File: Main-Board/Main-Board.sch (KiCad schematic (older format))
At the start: 1 part

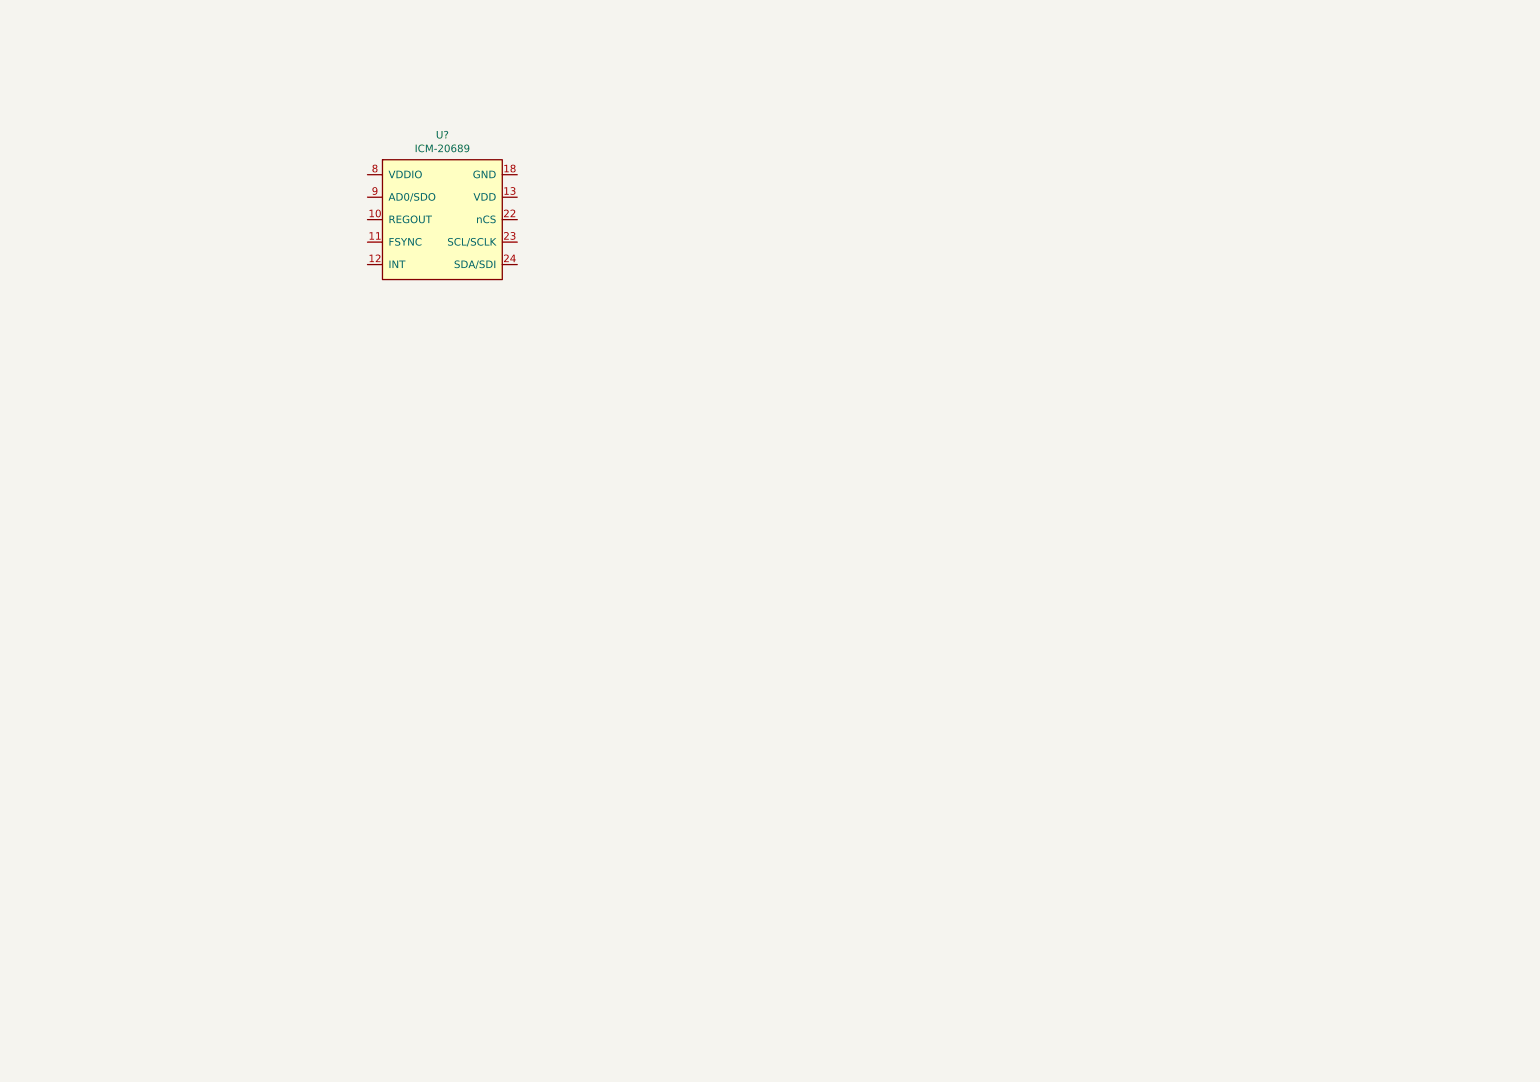
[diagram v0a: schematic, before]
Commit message: roughed out the imu schematic
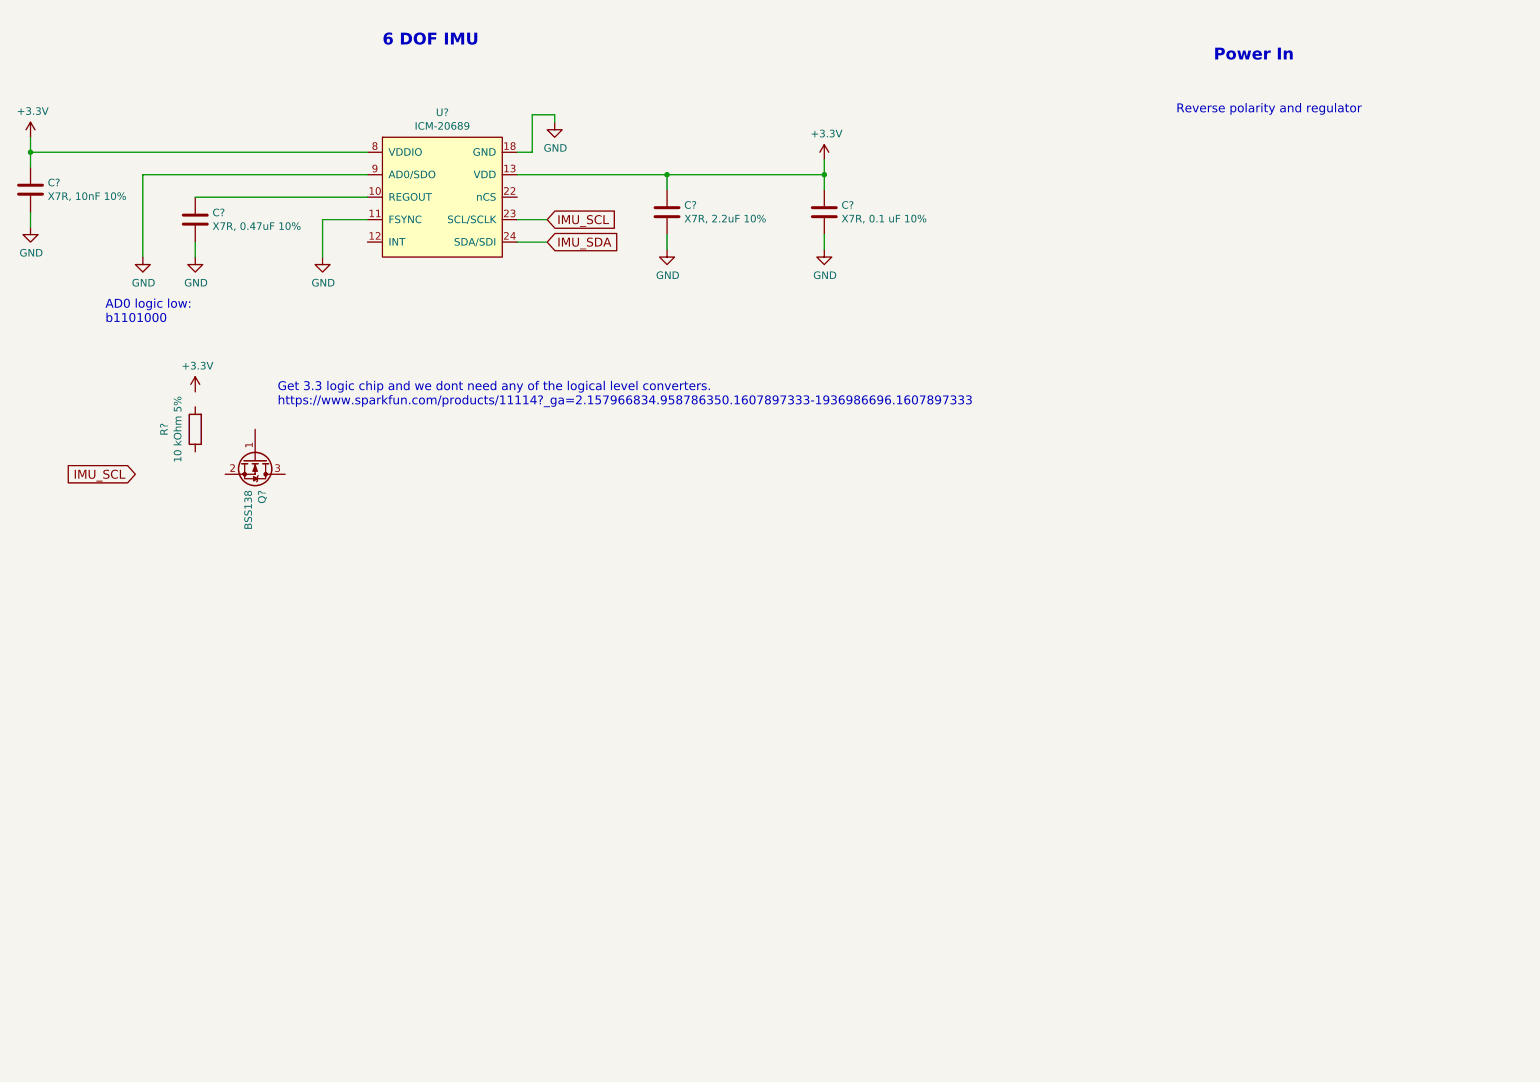
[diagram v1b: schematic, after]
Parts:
- added C?: X7R, 0.47uF 10%, Capacitor_SMD:C_0603_1608Metric_Pad1.05x0.95mm_HandSolder, symbol Device:C
- added C?: X7R, 0.1 uF 10%, Capacitor_SMD:C_0603_1608Metric_Pad1.05x0.95mm_HandSolder, symbol Device:C
- added C?: X7R, 2.2uF 10%, Capacitor_SMD:C_0603_1608Metric_Pad1.05x0.95mm_HandSolder, symbol Device:C
- added C?: X7R, 10nF 10%, Capacitor_SMD:C_0603_1608Metric_Pad1.05x0.95mm_HandSolder, symbol Device:C
- added Q?: BSS138, Package_TO_SOT_SMD:SOT-23, symbol Transistor_FET:BSS138
- added R?: 10 kOhm 5%, symbol Device:R
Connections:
- net at U?.10 (REGOUT): now also C?.1
- net GND: now reaches U?.11 (FSYNC)
- net GND: now also U?.18 (GND), U?.9 (AD0/SDO), C?.2, C?.2, C?.2, C?.2
- net +3V3: now reaches U?.13 (VDD)
- net +3V3: now also U?.8 (VDDIO), C?.1, C?.1, C?.1
- net IMU_SCL: now reaches U?.23 (SCL/SCLK)
- net IMU_SDA: now reaches U?.24 (SDA/SDI)
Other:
- note added: "6 DOF IMU"
- note added: "AD0 logic low: \nb1101000"
- note added: "Get 3.3 logic chip and we dont need any of the logical level converters. \nhttps://www.sparkfun.com/products/11114?_ga=2.157966834.958786350.1607897333-1936986696.1607897333"
- note added: "Power In"
- note added: "Reverse polarity and regulator"
- moved on the sheet: U?

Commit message: Select ATMEGA328P as main processor, started to route.
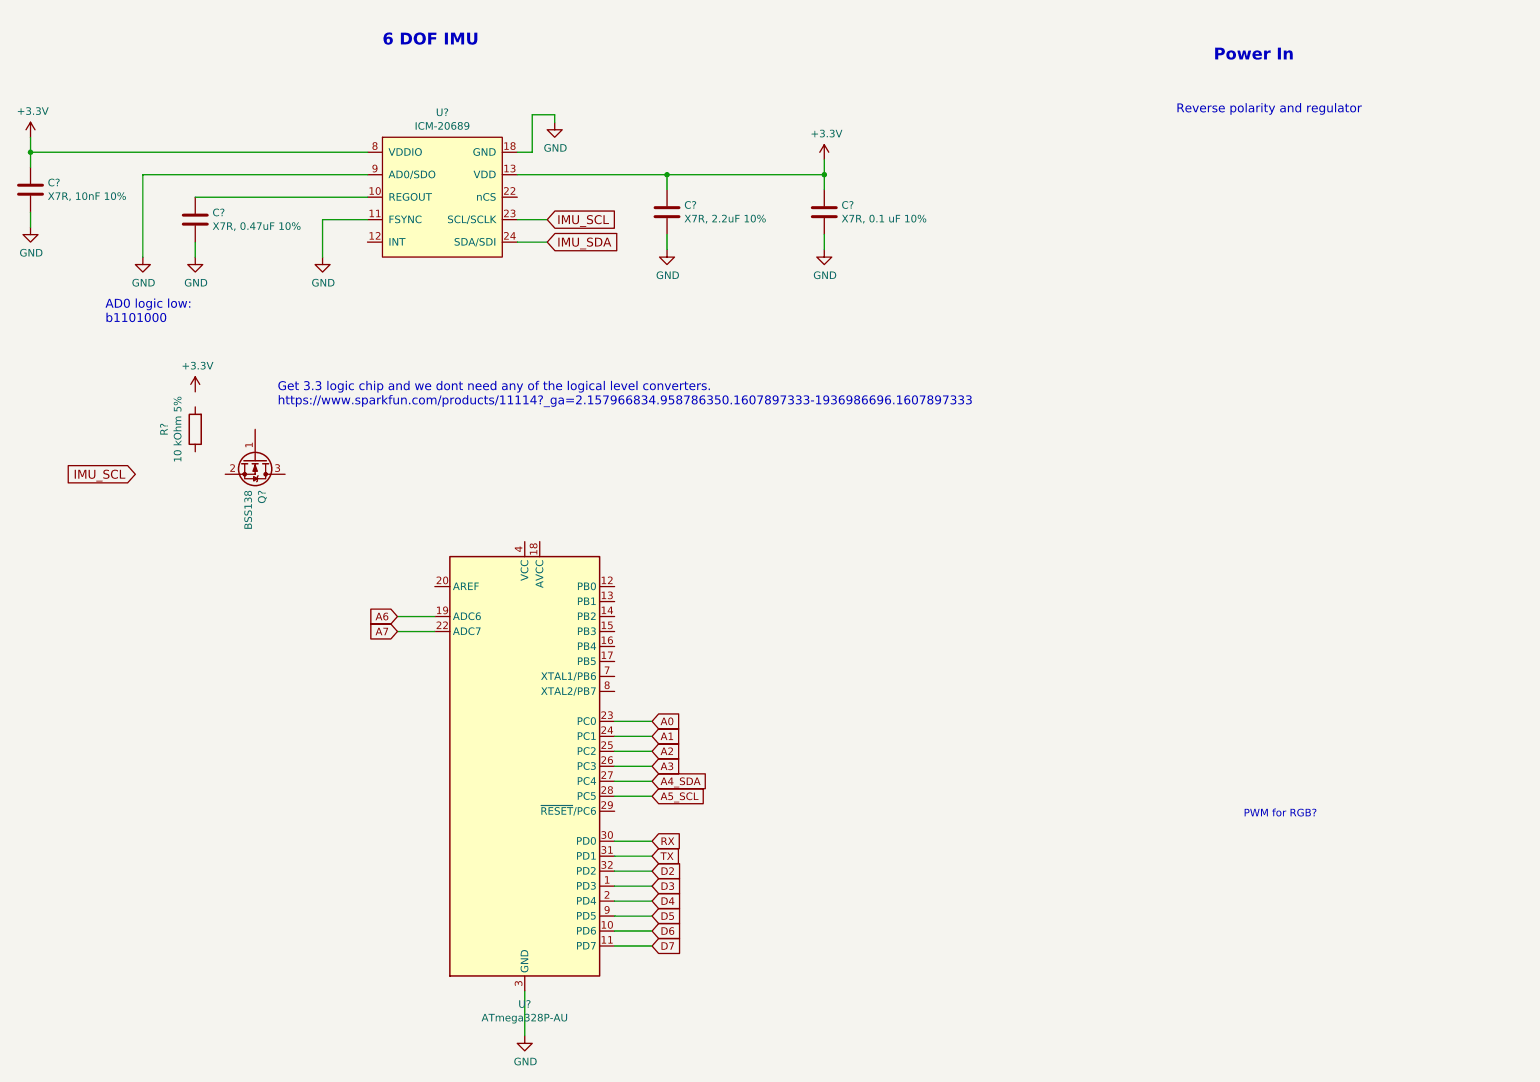
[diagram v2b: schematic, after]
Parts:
- added U?: ATmega328P-AU, Package_QFP:TQFP-32_7x7mm_P0.8mm, symbol MCU_Microchip_ATmega:ATmega328P-AU
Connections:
- net GND: now also U?.21 (GND), U?.3 (GND), U?.5 (GND)
- new net: U?.4 (VCC), U?.6 (VCC)
- new net A0: U?.23 (PC0)
- new net A1: U?.24 (PC1)
- new net A2: U?.25 (PC2)
- new net A3: U?.26 (PC3)
- new net A4_SDA: U?.27 (PC4)
- new net A5_SCL: U?.28 (PC5)
- new net A6: U?.19 (ADC6)
- new net A7: U?.22 (ADC7)
- new net D2: U?.32 (PD2)
- new net D3: U?.1 (PD3)
- new net D4: U?.2 (PD4)
- new net D5: U?.9 (PD5)
- new net D6: U?.10 (PD6)
- new net D7: U?.11 (PD7)
- new net RX: U?.30 (PD0)
- new net TX: U?.31 (PD1)
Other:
- note added: "PWM for RGB?"
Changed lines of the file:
@@
 EESchema Schematic File Version 4
+LIBS:Main-Board-cache
 EELAYER 30 0
 EELAYER END
@@
 Text Notes 2300 3250 0    59   ~ 0
 Get 3.3 logic chip and we dont need any of the logical level converters. \nhttps://www.sparkfun.com/products/11114?_ga=2.157966834.958786350.1607897333-1936986696.1607897333
+$Comp
+L MCU_Microchip_ATmega:ATmega328P-AU U?
+U 1 1 5FD850AB
+P 3950 5650
+F 0 "U?" H 3950 4061 50  0000 C CNN
+F 1 "ATmega328P-AU" H 3950 3970 50  0000 C CNN
+F 2 "Package_QFP:TQFP-32_7x7mm_P0.8mm" H 3950 5650 50  0001 C CIN
+F 3 "http://ww1.microchip.com/downloads/en/DeviceDoc/ATmega328_P%20AVR%20MCU%20with%20picoPower%20Technology%20Data%20Sheet%2040001984A.pdf" H 3950 5650 50  0001 C CNN
+	1    3950 5650
+	1    0    0    -1
+$EndComp
+Text GLabel 4800 5350 2    50   Input ~ 0
+A0
+Text GLabel 4800 5450 2    50   Input ~ 0
+A1
+Text GLabel 3100 4750 0    50   Input ~ 0
+A7
+Text GLabel 3100 4650 0    50   Input ~ 0
+A6
+Wire Wire Line
+	3100 4650 3350 4650
+Wire Wire Line
+	3350 4750 3100 4750
+Wire Wire Line
+	4800 5350 4550 5350
+Wire Wire Line
+	4800 5450 4550 5450
+Text GLabel 4800 5550 2    50   Input ~ 0
+A2
+Wire Wire Line
+	4800 5550 4550 5550
+Text GLabel 4800 5650 2    50   Input ~ 0
+A3
+Wire Wire Line
+	4800 5650 4550 5650
+Text GLabel 4800 5750 2    50   Input ~ 0
+A4_SDA
+Text GLabel 4800 5850 2    50   Input ~ 0
+A5_SCL
+Wire Wire Line
+	4550 5750 4800 5750
+Wire Wire Line
+	4800 5850 4550 5850
+$Comp
+L power:GND #PWR?
+U 1 1 5FD8ADF7
+P 3950 7450
+F 0 "#PWR?" H 3950 7200 50  0001 C CNN
+F 1 "GND" H 3955 7277 50  0000 C CNN
+F 2 "" H 3950 7450 50  0001 C CNN
+F 3 "" H 3950 7450 50  0001 C CNN
+	1    3950 7450
+	1    0    0    -1
+$EndComp
+Wire Wire Line
+	3950 7450 3950 7150
+Text GLabel 4800 6150 2    50   Input ~ 0
+RX
+Text GLabel 4800 6250 2    50   Input ~ 0
+TX
+Wire Wire Line
+	4550 6150 4800 6150
+Wire Wire Line
+	4800 6250 4550 6250
+Text GLabel 4800 6350 2    50   Input ~ 0
+D2
+Text GLabel 4800 6450 2    50   Input ~ 0
+D3
+Text GLabel 4800 6550 2    50   Input ~ 0
+D4
+Text GLabel 4800 6650 2    50   Input ~ 0
+D5
+Text GLabel 4800 6750 2    50   Input ~ 0
+D6
+Text GLabel 4800 6850 2    50   Input ~ 0
+D7
+Wire Wire Line
+	4550 6850 4800 6850
+Wire Wire Line
+	4800 6750 4550 6750
+Wire Wire Line
+	4550 6650 4800 6650
+Wire Wire Line
+	4800 6550 4550 6550
+Wire Wire Line
+	4550 6450 4800 6450
+Wire Wire Line
+	4800 6350 4550 6350
+Text Notes 8750 6000 0    50   ~ 0
+PWM for RGB?
 $EndSCHEMATC

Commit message: Gave everything their own sheet and made schematic for USB interface. USE 5 v logic for now
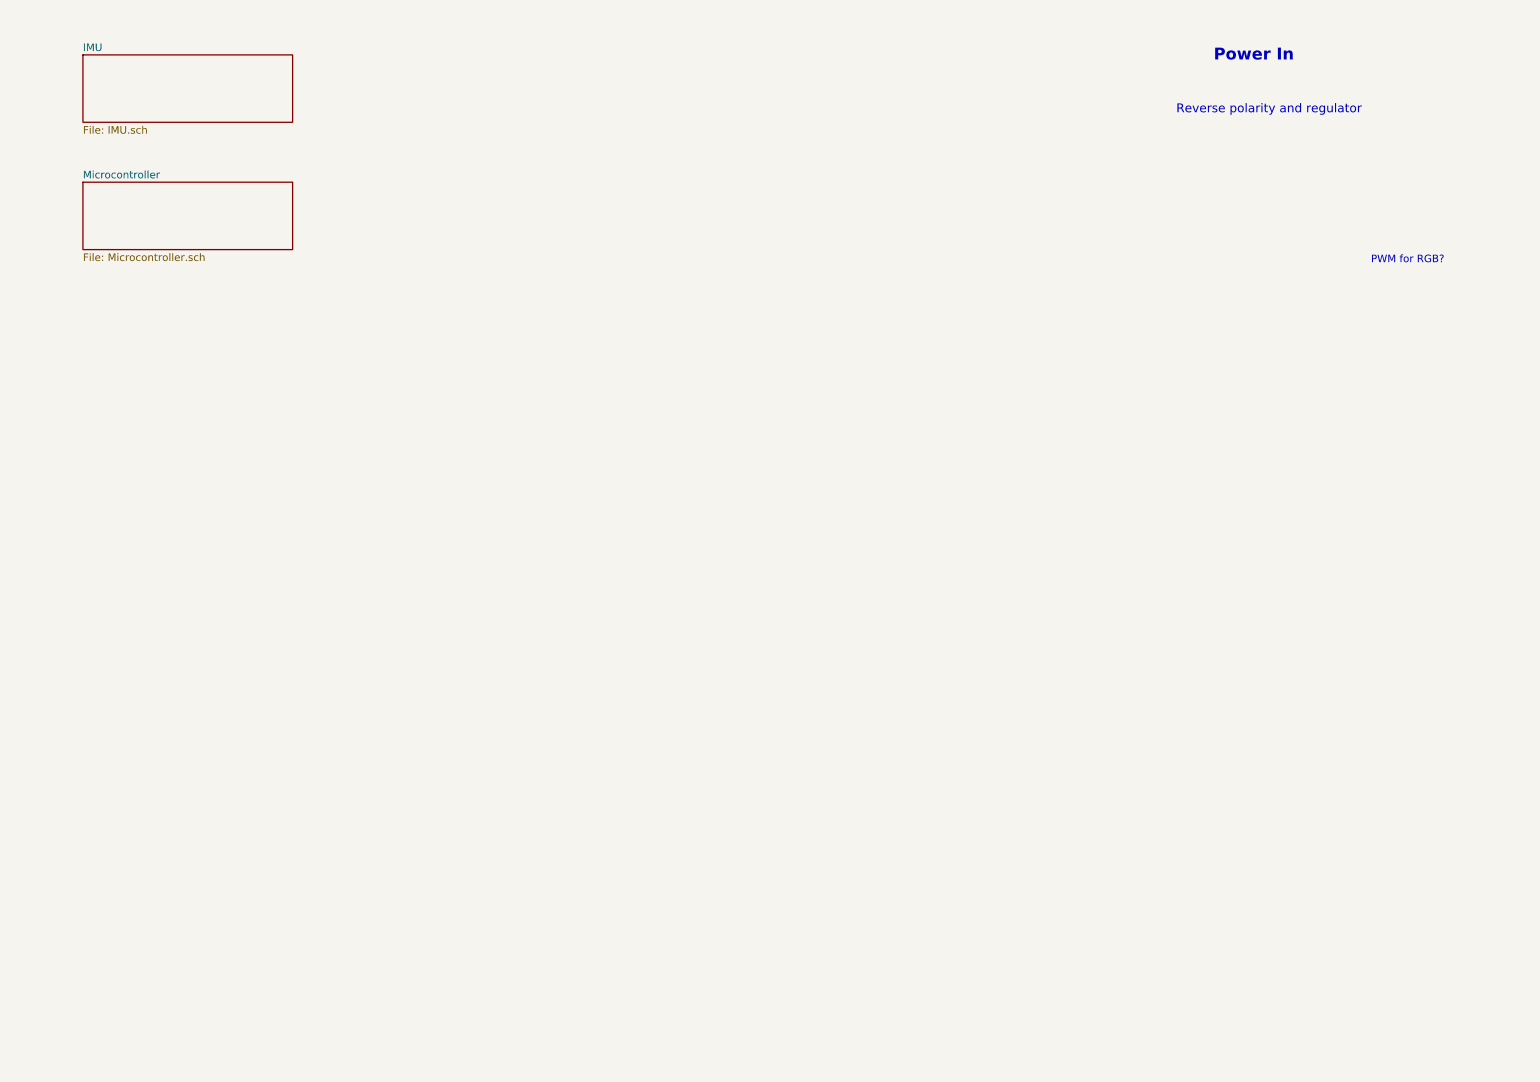
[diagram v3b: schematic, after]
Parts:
- removed C?: X7R, 0.47uF 10%, Capacitor_SMD:C_0603_1608Metric_Pad1.05x0.95mm_HandSolder, symbol Device:C
- removed C?: X7R, 0.1 uF 10%, Capacitor_SMD:C_0603_1608Metric_Pad1.05x0.95mm_HandSolder, symbol Device:C
- removed C?: X7R, 2.2uF 10%, Capacitor_SMD:C_0603_1608Metric_Pad1.05x0.95mm_HandSolder, symbol Device:C
- removed C?: X7R, 10nF 10%, Capacitor_SMD:C_0603_1608Metric_Pad1.05x0.95mm_HandSolder, symbol Device:C
- removed Q?: BSS138, Package_TO_SOT_SMD:SOT-23, symbol Transistor_FET:BSS138
- removed R?: 10 kOhm 5%, symbol Device:R
- removed U?: ICM-20689, Package_DFN_QFN:QFN-24-1EP_4x4mm_P0.5mm_EP2.8x2.8mm, symbol Custom:ICM-20689
- removed U?: ATmega328P-AU, Package_QFP:TQFP-32_7x7mm_P0.8mm, symbol MCU_Microchip_ATmega:ATmega328P-AU
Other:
- note removed: "6 DOF IMU"
- note removed: "AD0 logic low: \nb1101000"
- note removed: "Get 3.3 logic chip and we dont need any of the logical level converters. \nhttps://www.sparkfun.com/products/11114?_ga=2.157966834.958786350.1607897333-1936986696.1607897333"

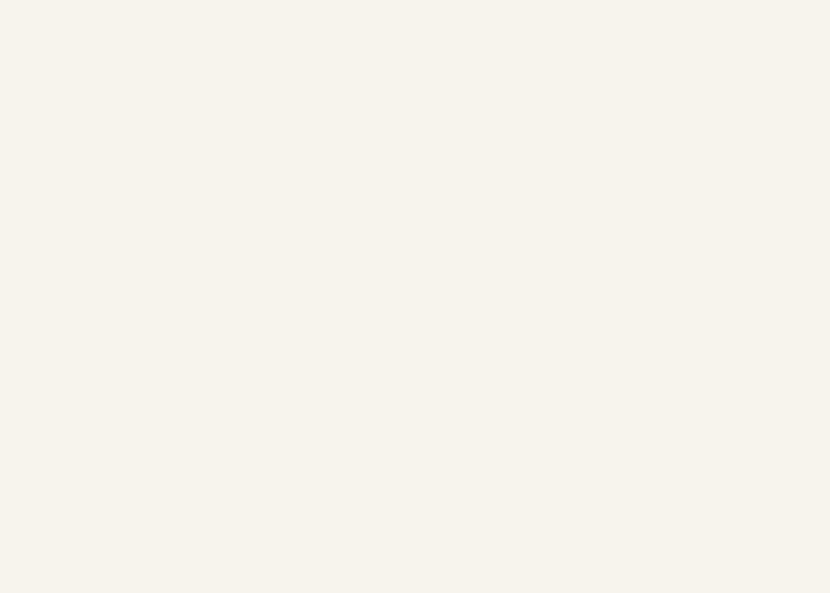
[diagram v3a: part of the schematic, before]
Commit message: Added in microcontroller voltage regulation
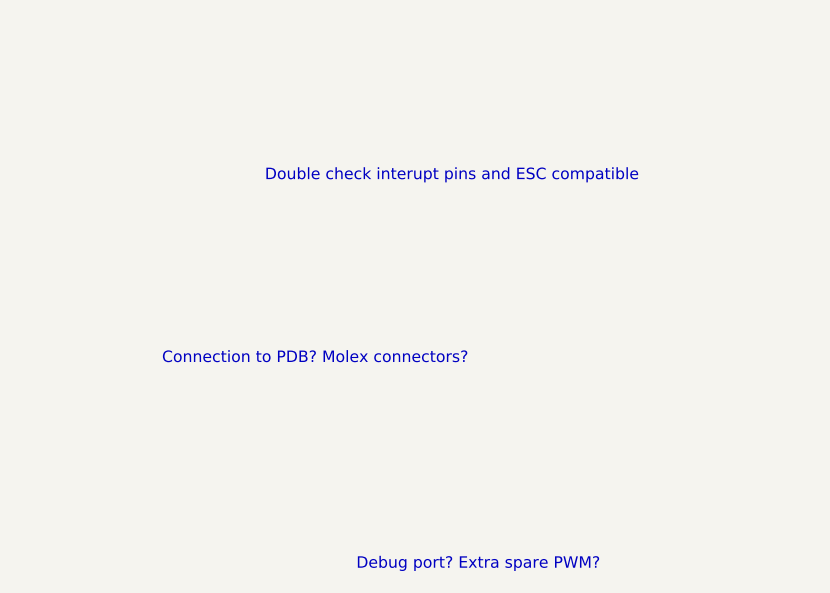
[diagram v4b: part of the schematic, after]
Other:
- note added: "Connection to PDB? Molex connectors?"
- note added: "Debug port? Extra spare PWM?\n"
- note added: "Double check interupt pins and ESC compatible"
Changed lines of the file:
@@
 F1 "Microcontroller.sch" 50
 $EndSheet
+Text Notes 7850 3150 0    50   ~ 0
+Double check interupt pins and ESC compatible
+Text Notes 7400 3950 0    50   ~ 0
+Connection to PDB? Molex connectors?
+Text Notes 8250 4850 0    50   ~ 0
+Debug port? Extra spare PWM?\n
 $EndSCHEMATC
